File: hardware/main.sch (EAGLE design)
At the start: 100 parts, among them IC1 MPU-6050, IC2 TB6612FNG, M1 MOTOR_MOUNT_V2, M2 LED_MOUNT, M3 LED_MOUNT, M4 LED_MOUNT, M5 LED_MOUNT, M6 LED_MOUNT, M7 LED_MOUNT, Q7 IRLML2244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

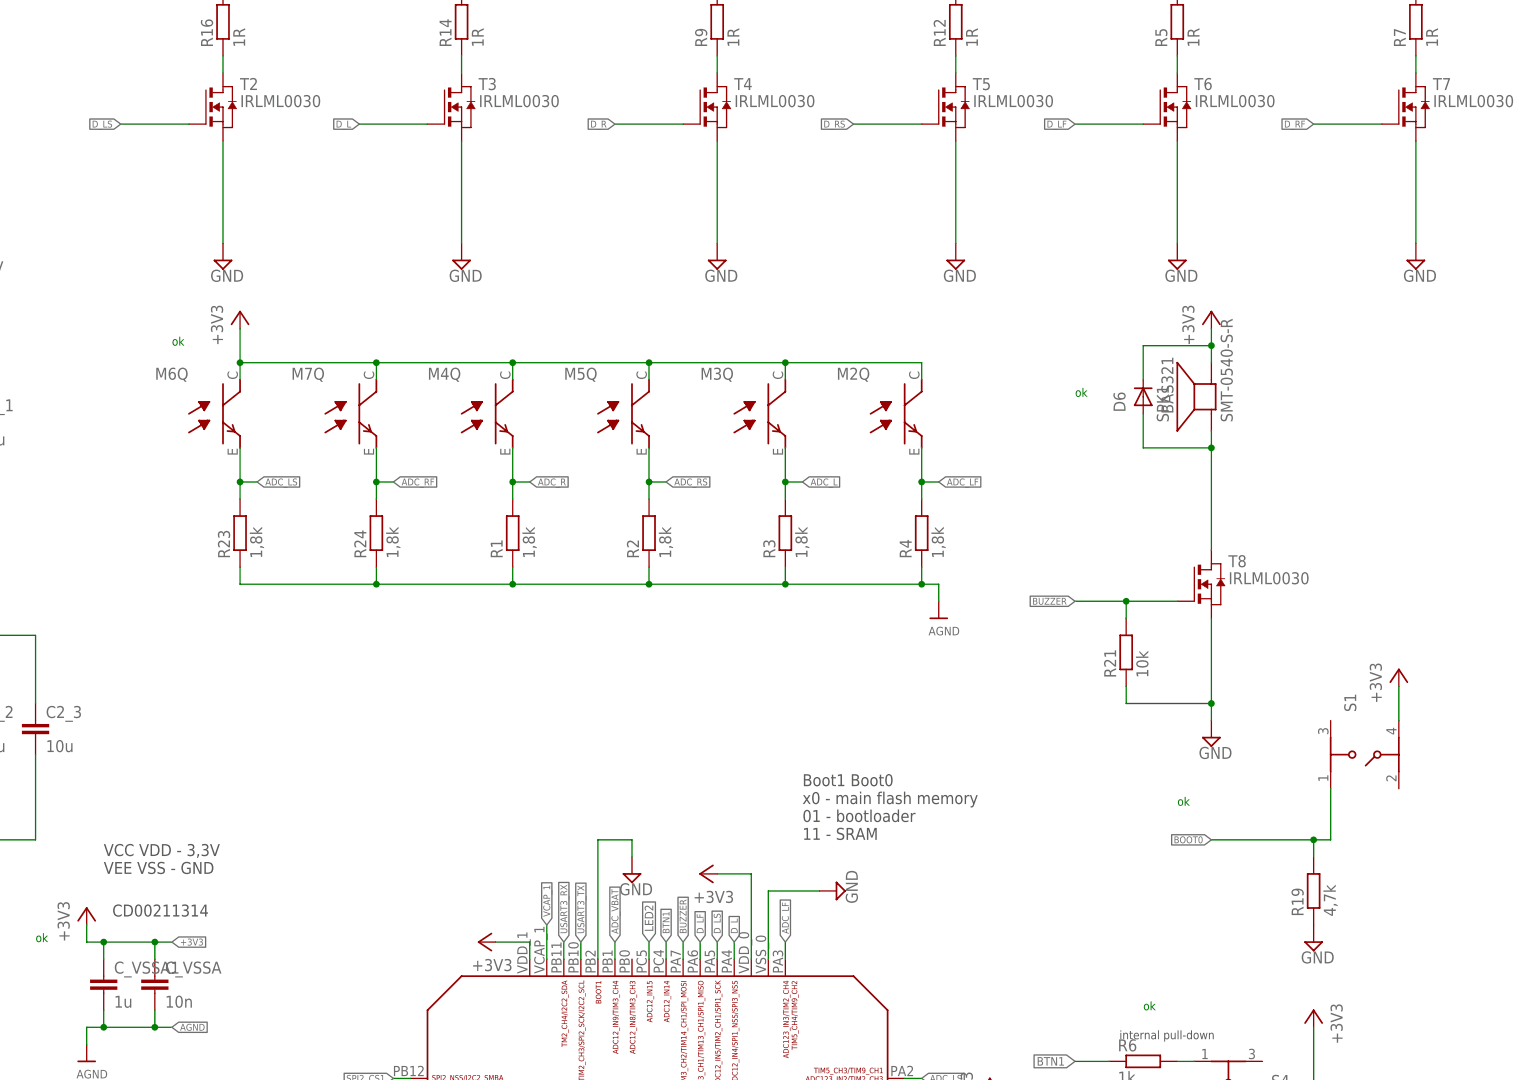
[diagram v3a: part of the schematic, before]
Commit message: added mosfet pulldowns (IR leds), PB2 pulldown
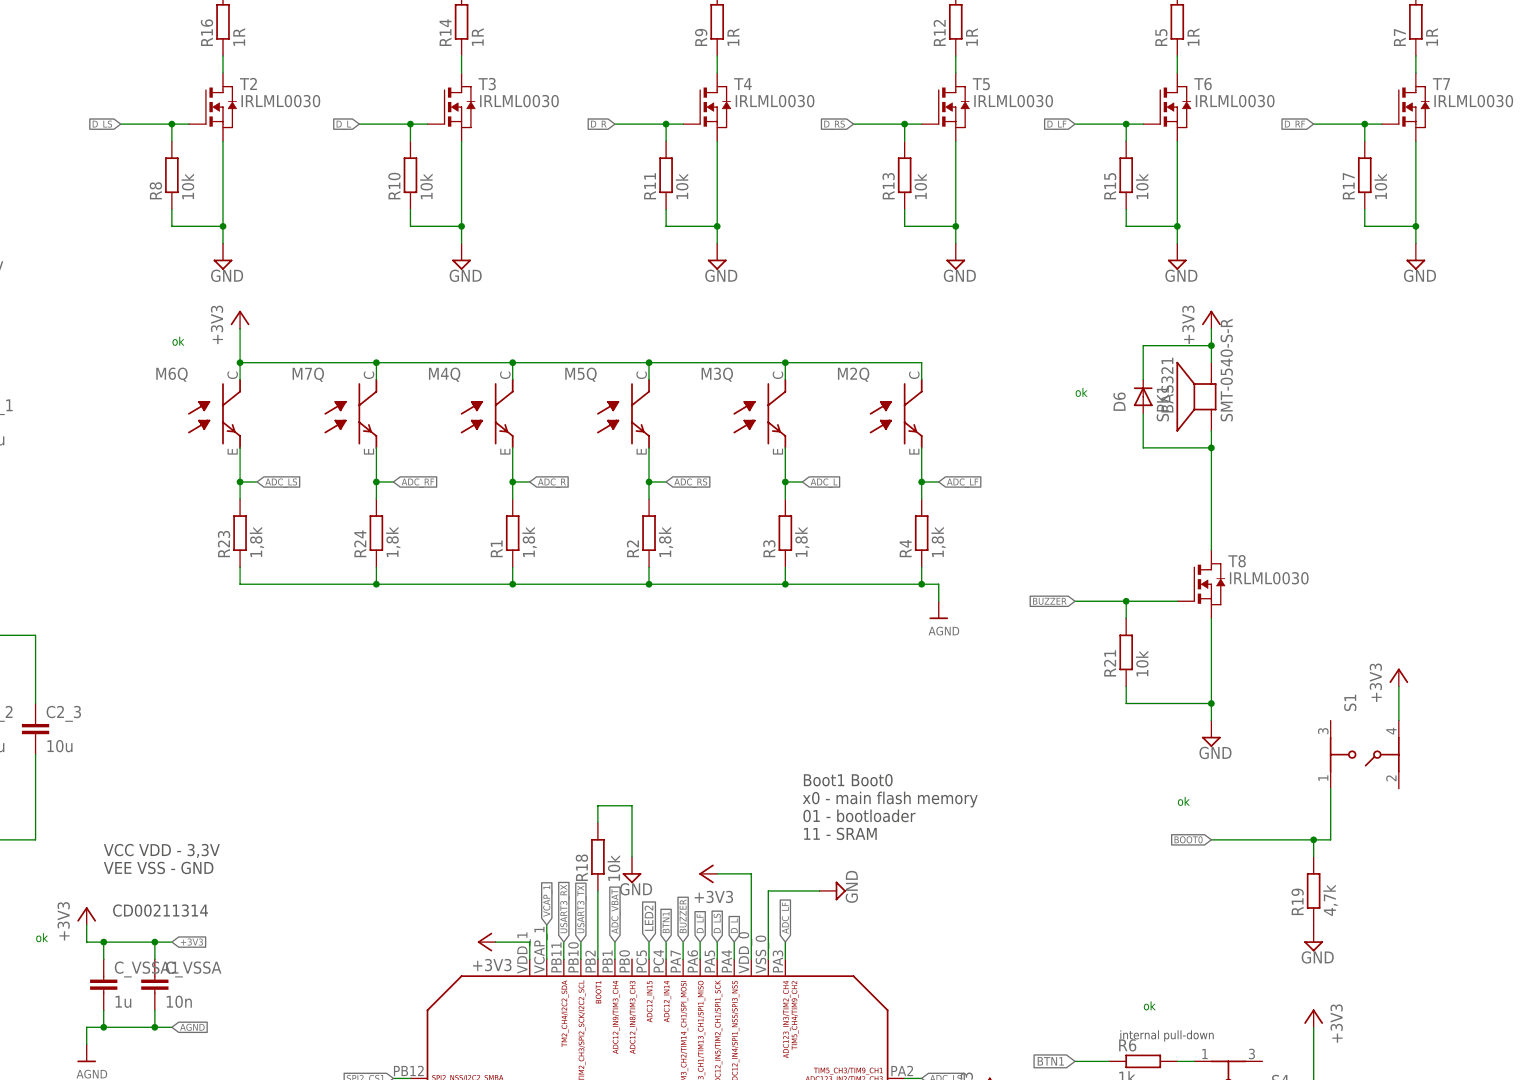
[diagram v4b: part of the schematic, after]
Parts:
- added R10, R11, R13, R15, R17, R18, R8: 10k, rcl:R-EU_R0603
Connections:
- new net N$3: R18.1, U3.PB2
- net D_L: now also R10.2
- net D_LF: now also R15.2
- net D_LS: now also R8.2
- net D_R: now also R11.2
- net D_RF: now also R17.2
- net D_RS: now also R13.2
- net GND: now also R10.1, R11.1, R13.1, R15.1, R17.1, R18.2, R8.1; no longer U3.PB2
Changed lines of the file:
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@@
 <part name="+3V28" library="supply1" deviceset="+3V3" device=""/>
 <part name="C1_3" library="rcl" deviceset="C-EU" device="C0805" value="10u"/>
+<part name="R8" library="rcl" deviceset="R-EU_" device="R0603" value="10k"/>
+<part name="R10" library="rcl" deviceset="R-EU_" device="R0603" value="10k"/>
+<part name="R11" library="rcl" deviceset="R-EU_" device="R0603" value="10k"/>
+<part name="R13" library="rcl" deviceset="R-EU_" device="R0603" value="10k"/>
+<part name="R15" library="rcl" deviceset="R-EU_" device="R0603" value="10k"/>
+<part name="R17" library="rcl" deviceset="R-EU_" device="R0603" value="10k"/>
+<part name="R18" library="rcl" deviceset="R-EU_" device="R0603" value="10k"/>
 </parts>
 <sheets>
@@
 <instance part="+3V28" gate="G$1" x="137.16" y="5.08"/>
 <instance part="C1_3" gate="G$1" x="-144.78" y="139.7"/>
+<instance part="R8" gate="G$1" x="-22.86" y="200.66" rot="R90"/>
+<instance part="R10" gate="G$1" x="12.7" y="200.66" rot="R90"/>
+<instance part="R11" gate="G$1" x="50.8" y="200.66" rot="R90"/>
+<instance part="R13" gate="G$1" x="86.36" y="200.66" rot="R90"/>
+<instance part="R15" gate="G$1" x="119.38" y="200.66" rot="R90"/>
+<instance part="R17" gate="G$1" x="154.94" y="200.66" rot="R90"/>
+<instance part="R18" gate="G$1" x="40.64" y="99.06" rot="R90"/>
 </instances>
 <busses>
@@
 <segment>
 <pinref part="T6" gate="A" pin="S"/>
-<wire x1="127" y1="205.74" x2="127" y2="190.5" width="0.1524" layer="91"/>
+<wire x1="127" y1="205.74" x2="127" y2="193.04" width="0.1524" layer="91"/>
 <pinref part="AGND4" gate="GND" pin="GND"/>
+<pinref part="R15" gate="G$1" pin="1"/>
+<wire x1="127" y1="193.04" x2="127" y2="190.5" width="0.1524" layer="91"/>
+<wire x1="119.38" y1="195.58" x2="119.38" y2="193.04" width="0.1524" layer="91"/>
+<wire x1="119.38" y1="193.04" x2="127" y2="193.04" width="0.1524" layer="91"/>
+<junction x="127" y="193.04"/>
 </segment>
 <segment>
@@
 <segment>
 <pinref part="T7" gate="A" pin="S"/>
-<wire x1="162.56" y1="205.74" x2="162.56" y2="190.5" width="0.1524" layer="91"/>
+<wire x1="162.56" y1="205.74" x2="162.56" y2="193.04" width="0.1524" layer="91"/>
 <pinref part="AGND7" gate="GND" pin="GND"/>
+<pinref part="R17" gate="G$1" pin="1"/>
+<wire x1="162.56" y1="193.04" x2="162.56" y2="190.5" width="0.1524" layer="91"/>
+<wire x1="154.94" y1="195.58" x2="154.94" y2="193.04" width="0.1524" layer="91"/>
+<wire x1="154.94" y1="193.04" x2="162.56" y2="193.04" width="0.1524" layer="91"/>
+<junction x="162.56" y="193.04"/>
 </segment>
 <segment>
 <pinref part="T4" gate="A" pin="S"/>
-<wire x1="58.42" y1="205.74" x2="58.42" y2="190.5" width="0.1524" layer="91"/>
+<wire x1="58.42" y1="205.74" x2="58.42" y2="193.04" width="0.1524" layer="91"/>
 <pinref part="AGND8" gate="GND" pin="GND"/>
+<pinref part="R11" gate="G$1" pin="1"/>
+<wire x1="58.42" y1="193.04" x2="58.42" y2="190.5" width="0.1524" layer="91"/>
+<wire x1="50.8" y1="195.58" x2="50.8" y2="193.04" width="0.1524" layer="91"/>
+<wire x1="50.8" y1="193.04" x2="58.42" y2="193.04" width="0.1524" layer="91"/>
+<junction x="58.42" y="193.04"/>
 </segment>
 <segment>
 <pinref part="T5" gate="A" pin="S"/>
-<wire x1="93.98" y1="205.74" x2="93.98" y2="190.5" width="0.1524" layer="91"/>
+<wire x1="93.98" y1="205.74" x2="93.98" y2="193.04" width="0.1524" layer="91"/>
 <pinref part="AGND9" gate="GND" pin="GND"/>
+<pinref part="R13" gate="G$1" pin="1"/>
+<wire x1="93.98" y1="193.04" x2="93.98" y2="190.5" width="0.1524" layer="91"/>
+<wire x1="86.36" y1="195.58" x2="86.36" y2="193.04" width="0.1524" layer="91"/>
+<wire x1="86.36" y1="193.04" x2="93.98" y2="193.04" width="0.1524" layer="91"/>
+<junction x="93.98" y="193.04"/>
 </segment>
 <segment>
 <pinref part="T3" gate="A" pin="S"/>
-<wire x1="20.32" y1="205.74" x2="20.32" y2="190.5" width="0.1524" layer="91"/>
+<wire x1="20.32" y1="205.74" x2="20.32" y2="193.04" width="0.1524" layer="91"/>
 <pinref part="AGND10" gate="GND" pin="GND"/>
+<pinref part="R10" gate="G$1" pin="1"/>
+<wire x1="20.32" y1="193.04" x2="20.32" y2="190.5" width="0.1524" layer="91"/>
+<wire x1="12.7" y1="195.58" x2="12.7" y2="193.04" width="0.1524" layer="91"/>
+<wire x1="12.7" y1="193.04" x2="20.32" y2="193.04" width="0.1524" layer="91"/>
+<junction x="20.32" y="193.04"/>
 </segment>
 <segment>
 <pinref part="T2" gate="A" pin="S"/>
-<wire x1="-15.24" y1="205.74" x2="-15.24" y2="190.5" width="0.1524" layer="91"/>
+<wire x1="-15.24" y1="205.74" x2="-15.24" y2="193.04" width="0.1524" layer="91"/>
 <pinref part="AGND11" gate="GND" pin="GND"/>
+<pinref part="R8" gate="G$1" pin="1"/>
+<wire x1="-15.24" y1="193.04" x2="-15.24" y2="190.5" width="0.1524" layer="91"/>
+<wire x1="-22.86" y1="195.58" x2="-22.86" y2="193.04" width="0.1524" layer="91"/>
+<wire x1="-22.86" y1="193.04" x2="-15.24" y2="193.04" width="0.1524" layer="91"/>
+<junction x="-15.24" y="193.04"/>
 </segment>
 <segment>
@@
 </segment>
 <segment>
-<pinref part="U3" gate="G$1" pin="PB2"/>
-<wire x1="40.64" y1="83.82" x2="40.64" y2="101.6" width="0.1524" layer="91"/>
-<wire x1="40.64" y1="101.6" x2="45.72" y2="101.6" width="0.1524" layer="91"/>
-<wire x1="45.72" y1="101.6" x2="45.72" y2="99.06" width="0.1524" layer="91"/>
 <pinref part="AGND36" gate="GND" pin="GND"/>
+<pinref part="R18" gate="G$1" pin="2"/>
+<wire x1="40.64" y1="104.14" x2="40.64" y2="106.68" width="0.1524" layer="91"/>
+<wire x1="40.64" y1="106.68" x2="45.72" y2="106.68" width="0.1524" layer="91"/>
+<wire x1="45.72" y1="106.68" x2="45.72" y2="99.06" width="0.1524" layer="91"/>
 </segment>
 <segment>
@@
 <label x="-30.48" y="208.28" size="1.016" layer="95" rot="R180" xref="yes"/>
 <pinref part="T2" gate="A" pin="G"/>
-<wire x1="-20.32" y1="208.28" x2="-30.48" y2="208.28" width="0.1524" layer="91"/>
+<wire x1="-20.32" y1="208.28" x2="-22.86" y2="208.28" width="0.1524" layer="91"/>
+<pinref part="R8" gate="G$1" pin="2"/>
+<wire x1="-22.86" y1="208.28" x2="-30.48" y2="208.28" width="0.1524" layer="91"/>
+<wire x1="-22.86" y1="205.74" x2="-22.86" y2="208.28" width="0.1524" layer="91"/>
+<junction x="-22.86" y="208.28"/>
 </segment>
 <segment>
@@
 <label x="5.08" y="208.28" size="1.016" layer="95" rot="R180" xref="yes"/>
 <pinref part="T3" gate="A" pin="G"/>
-<wire x1="15.24" y1="208.28" x2="5.08" y2="208.28" width="0.1524" layer="91"/>
+<wire x1="15.24" y1="208.28" x2="12.7" y2="208.28" width="0.1524" layer="91"/>
+<pinref part="R10" gate="G$1" pin="2"/>
+<wire x1="12.7" y1="208.28" x2="5.08" y2="208.28" width="0.1524" layer="91"/>
+<wire x1="12.7" y1="205.74" x2="12.7" y2="208.28" width="0.1524" layer="91"/>
+<junction x="12.7" y="208.28"/>
 </segment>
 </net>
@@
 <label x="147.32" y="208.28" size="1.016" layer="95" rot="R180" xref="yes"/>
 <pinref part="T7" gate="A" pin="G"/>
-<wire x1="157.48" y1="208.28" x2="147.32" y2="208.28" width="0.1524" layer="91"/>
+<wire x1="157.48" y1="208.28" x2="154.94" y2="208.28" width="0.1524" layer="91"/>
+<pinref part="R17" gate="G$1" pin="2"/>
+<wire x1="154.94" y1="208.28" x2="147.32" y2="208.28" width="0.1524" layer="91"/>
+<wire x1="154.94" y1="208.28" x2="154.94" y2="205.74" width="0.1524" layer="91"/>
+<junction x="154.94" y="208.28"/>
 </segment>
 <segment>
@@
 <label x="78.74" y="208.28" size="1.016" layer="95" rot="R180" xref="yes"/>
 <pinref part="T5" gate="A" pin="G"/>
-<wire x1="88.9" y1="208.28" x2="78.74" y2="208.28" width="0.1524" layer="91"/>
+<wire x1="88.9" y1="208.28" x2="86.36" y2="208.28" width="0.1524" layer="91"/>
+<pinref part="R13" gate="G$1" pin="2"/>
+<wire x1="86.36" y1="208.28" x2="78.74" y2="208.28" width="0.1524" layer="91"/>
+<wire x1="86.36" y1="205.74" x2="86.36" y2="208.28" width="0.1524" layer="91"/>
+<junction x="86.36" y="208.28"/>
 </segment>
 <segment>
@@
 <label x="111.76" y="208.28" size="1.016" layer="95" rot="R180" xref="yes"/>
 <pinref part="T6" gate="A" pin="G"/>
-<wire x1="121.92" y1="208.28" x2="111.76" y2="208.28" width="0.1524" layer="91"/>
+<wire x1="121.92" y1="208.28" x2="119.38" y2="208.28" width="0.1524" layer="91"/>
+<pinref part="R15" gate="G$1" pin="2"/>
+<wire x1="119.38" y1="208.28" x2="111.76" y2="208.28" width="0.1524" layer="91"/>
+<wire x1="119.38" y1="205.74" x2="119.38" y2="208.28" width="0.1524" layer="91"/>
+<junction x="119.38" y="208.28"/>
 </segment>
 <segment>
@@
 <label x="43.18" y="208.28" size="1.016" layer="95" rot="R180" xref="yes"/>
 <pinref part="T4" gate="A" pin="G"/>
-<wire x1="53.34" y1="208.28" x2="43.18" y2="208.28" width="0.1524" layer="91"/>
+<wire x1="53.34" y1="208.28" x2="50.8" y2="208.28" width="0.1524" layer="91"/>
+<pinref part="R11" gate="G$1" pin="2"/>
+<wire x1="50.8" y1="208.28" x2="43.18" y2="208.28" width="0.1524" layer="91"/>
+<wire x1="50.8" y1="205.74" x2="50.8" y2="208.28" width="0.1524" layer="91"/>
+<junction x="50.8" y="208.28"/>
 </segment>
 </net>
@@
 </segment>
 </net>
+<net name="N$3" class="0">
+<segment>
+<pinref part="U3" gate="G$1" pin="PB2"/>
+<wire x1="40.64" y1="83.82" x2="40.64" y2="93.98" width="0.1524" layer="91"/>
+<pinref part="R18" gate="G$1" pin="1"/>
+</segment>
+</net>

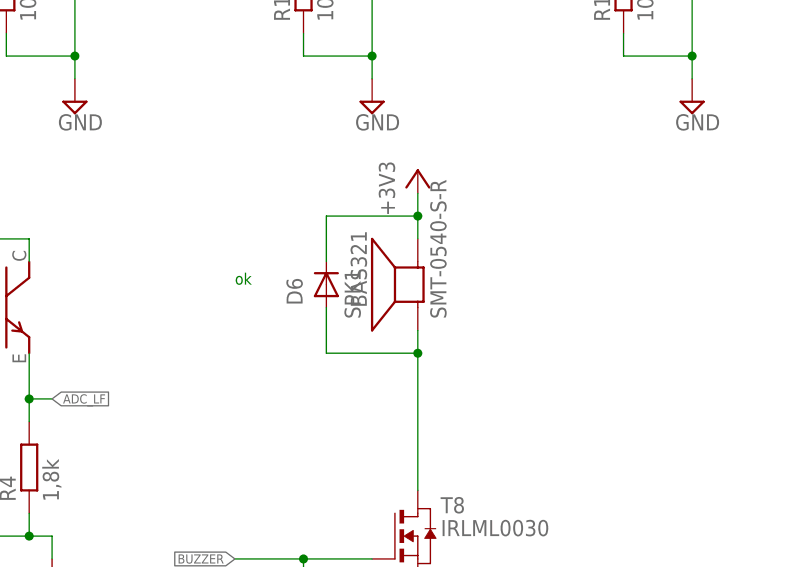
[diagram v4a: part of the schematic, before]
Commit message: fixed silkcreen covering pads
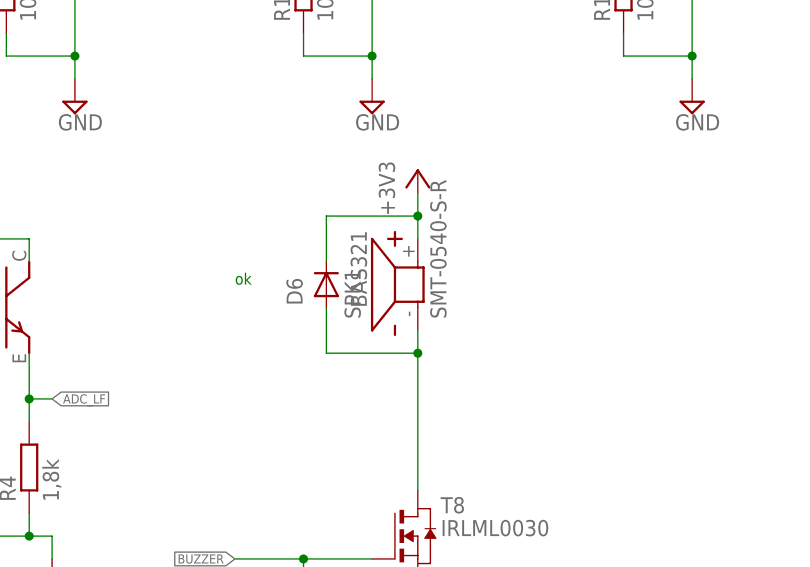
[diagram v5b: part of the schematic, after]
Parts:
- IC1: device invensense:MPU-6050 -> micromouse:MPU-6050
- SPK1: device adafruit:SMT-0540-S-R -> micromouse:SMT-0540-S-R
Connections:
- net +3V3: now also SPK1.+; no longer SPK1.-
- net N$30: now also SPK1.-; no longer SPK1.+
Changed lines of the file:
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@@
 <part name="T6" library="zetex" deviceset="NMOSSOT23" device="" value="IRLML0030"/>
 <part name="AGND4" library="supply2" deviceset="GND" device=""/>
-<part name="SPK1" library="adafruit" deviceset="SMT-0540-S-R" device=""/>
+<part name="SPK1" library="micromouse" deviceset="SMT-0540-S-R" device=""/>
 <part name="T8" library="zetex" deviceset="NMOSSOT23" device="" value="IRLML0030"/>
 <part name="AGND12" library="supply2" deviceset="GND" device=""/>
@@
 <part name="+3V3" library="supply1" deviceset="+3V3" device=""/>
 <part name="AGND14" library="supply2" deviceset="GND" device=""/>
-<part name="IC1" library="invensense" deviceset="MPU-6050" device=""/>
+<part name="IC1" library="micromouse" deviceset="MPU-6050" device=""/>
 <part name="C_VSSA1" library="rcl" deviceset="C-EU" device="C0603" value="1u"/>
 <part name="C25" library="rcl" deviceset="C-EU" device="C0603" value="100n"/>
@@
 <wire x1="121.92" y1="170.18" x2="121.92" y2="175.26" width="0.1524" layer="91"/>
 <wire x1="121.92" y1="175.26" x2="132.08" y2="175.26" width="0.1524" layer="91"/>
-<pinref part="SPK1" gate="G$1" pin="-"/>
+<pinref part="SPK1" gate="G$1" pin="+"/>
 <wire x1="132.08" y1="175.26" x2="132.08" y2="172.72" width="0.1524" layer="91"/>
 <junction x="132.08" y="175.26"/>
@@
 <pinref part="T8" gate="A" pin="D"/>
 <wire x1="132.08" y1="160.02" x2="132.08" y2="144.78" width="0.1524" layer="91"/>
-<pinref part="SPK1" gate="G$1" pin="+"/>
+<pinref part="SPK1" gate="G$1" pin="-"/>
 <wire x1="132.08" y1="160.02" x2="132.08" y2="162.56" width="0.1524" layer="91"/>
 <junction x="132.08" y="160.02"/>
